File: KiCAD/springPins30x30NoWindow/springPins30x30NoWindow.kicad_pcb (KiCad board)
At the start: 2 copper layers, 30 x 30 mm, 22 parts, among them J1 CONN_02X06, J2 CONN_02X06

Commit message: wip commit
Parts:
- moved R1 22.7 mm to (5.08, -10.2), turned to 0 degrees
- moved J1 16.3 mm to (6.35, -3.81), turned to 90 degrees
- moved J2 2.54 mm to (6.35, 6.35), turned to 90 degrees
- moved JP1 0.65 mm to (4.45, 10.2), turned to 270 degrees
- turned L1 to 180 degrees
- turned L1 to 0 degrees
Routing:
- net /I2: track 6.99 -> 24.7 mm
- net /V5: track 6.99 -> 24.5 mm
- net /V2: track 6.99 -> 21.3 mm
- net /I5: track 6.99 -> 21.2 mm
- net /I4: track 6.99 -> 17.8 mm
- net /V3: track 6.99 -> 17.6 mm
- net /VT: track 17.5 -> 6.99 mm
- net /IB: track 17.5 -> 6.99 mm
- net /V4: track 6.99 -> 14.0 mm
- net /I3: track 6.99 -> 13.9 mm
- net /VB: track 13.8 -> 6.99 mm
- net /IT: track 13.1 -> 6.99 mm
- net /I6: track 6.99 -> 12.0 mm
- net /RL: track 8.61 -> 3.84 mm
- net /V1: track 6.99 -> 11.0 mm
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
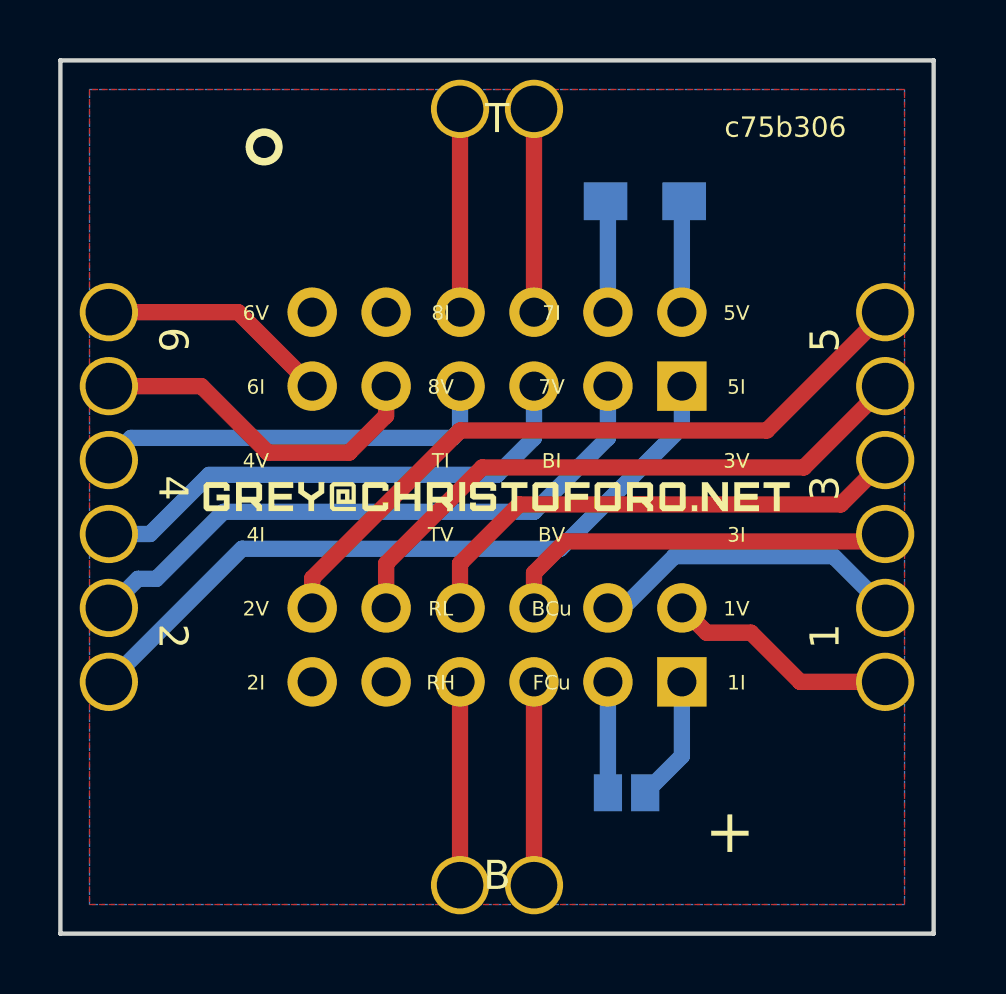
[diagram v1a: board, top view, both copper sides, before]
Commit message: rotate connectors on newMux
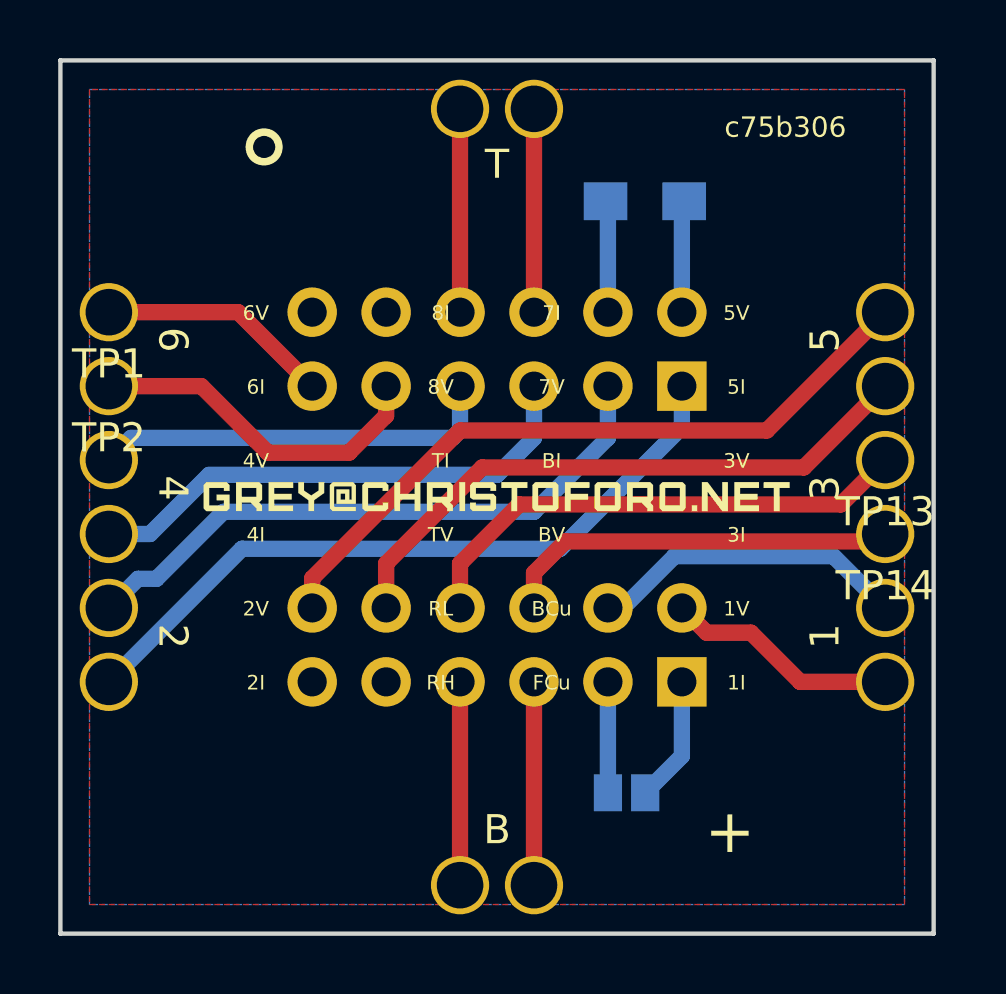
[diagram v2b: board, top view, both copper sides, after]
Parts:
- removed TP17, TP18, TP19, TP20: TEST, myParts:S25-022+P25-4023
- added TP1: TEST, myParts:S25-022+P25-4023, F.Cu at (-13.3, -6.35)
- added TP13: TEST, myParts:S25-022+P25-4023, F.Cu at (13.3, -1.27)
- added TP14: TEST, myParts:S25-022+P25-4023, F.Cu at (13.3, 1.27)
- added TP2: TEST, myParts:S25-022+P25-4023, F.Cu at (-13.3, -3.81)
- moved TP8 24.5 mm to (1.27, -13.3)
- moved TP12 21.0 mm to (13.3, -3.81)
- moved TP7 15.4 mm to (-1.27, 13.3)
- moved TP11 13.9 mm to (13.3, -6.35)
- moved TP15 10.2 mm to (13.3, 3.81)
- moved TP16 10.2 mm to (13.3, 6.35)
- moved TP3 5.08 mm to (-13.3, -1.27)
- moved TP4 5.08 mm to (-13.3, 1.27)
- moved TP5 5.08 mm to (-13.3, 3.81)
- moved TP6 5.08 mm to (-13.3, 6.35)
- moved TP10 2.54 mm to (1.27, 13.3)
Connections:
- TP10 pad 1: /IB -> /VB
- TP11 pad 1: /VT -> /V5
- TP12 pad 1: /VB -> /I5
- TP15 pad 1: /V5 -> /V1
- TP16 pad 1: /I5 -> /I1
- TP3 pad 1: /V6 -> /V4
- TP4 pad 1: /I6 -> /I4
- TP5 pad 1: /V4 -> /V2
- TP6 pad 1: /I4 -> /I2
- TP7 pad 1: /V2 -> /IB
- TP8 pad 1: /I2 -> /VT

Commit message: go back to old 30x30 springpins layout
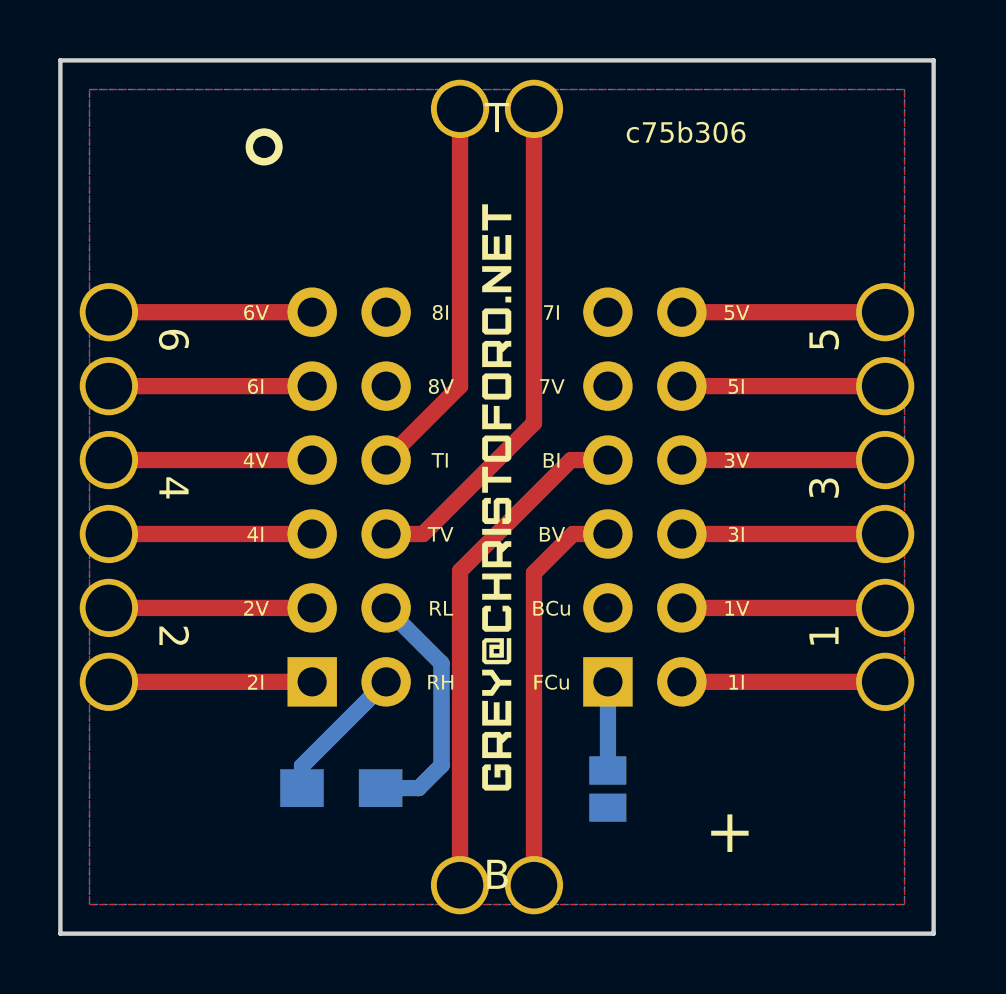
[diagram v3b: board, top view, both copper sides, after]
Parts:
- removed TP1, TP13, TP14, TP2: TEST, myParts:S25-022+P25-4023
- added TP17: TEST, myParts:S25-022+P25-4023, F.Cu at (13.3, -1.27)
- added TP18: TEST, myParts:S25-022+P25-4023, F.Cu at (13.3, 1.27)
- added TP19: TEST, myParts:S25-022+P25-4023, F.Cu at (13.3, 3.81)
- added TP20: TEST, myParts:S25-022+P25-4023, F.Cu at (13.3, 6.35)
- moved TP8 24.5 mm to (-13.3, 6.35)
- moved R1 22.7 mm to (-5.35, 10.0), turned to 180 degrees
- moved TP12 21.0 mm to (1.27, 13.3)
- moved J1 16.3 mm to (-6.35, 6.35), turned to 0 degrees
- moved TP7 15.4 mm to (-13.3, 3.81)
- moved TP11 13.9 mm to (1.27, -13.3)
- moved TP15 10.2 mm to (13.3, -6.35)
- moved TP16 10.2 mm to (13.3, -3.81)
- moved TP3 5.08 mm to (-13.3, -6.35)
- moved TP4 5.08 mm to (-13.3, -3.81)
- moved TP5 5.08 mm to (-13.3, -1.27)
- moved TP6 5.08 mm to (-13.3, 1.27)
- moved TP10 2.54 mm to (-1.27, 13.3)
- moved J2 2.54 mm to (3.81, 6.35), turned to 0 degrees
- moved JP1 0.65 mm to (3.81, 10.0), turned to 0 degrees
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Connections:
- TP10 pad 1: /VB -> /IB
- TP11 pad 1: /V5 -> /VT
- TP12 pad 1: /I5 -> /VB
- TP15 pad 1: /V1 -> /V5
- TP16 pad 1: /I1 -> /I5
- TP3 pad 1: /V4 -> /V6
- TP4 pad 1: /I4 -> /I6
- TP5 pad 1: /V2 -> /V4
- TP6 pad 1: /I2 -> /I4
- TP7 pad 1: /IB -> /V2
- TP8 pad 1: /VT -> /I2
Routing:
- net /I2: track 24.7 -> 6.99 mm
- net /V5: track 24.5 -> 6.99 mm
- net /V2: track 21.3 -> 6.99 mm
- net /I5: track 21.2 -> 6.99 mm
- net /I4: track 17.8 -> 6.99 mm
- net /V3: track 17.6 -> 6.99 mm
- net /VT: track 6.99 -> 17.5 mm
- net /IB: track 6.99 -> 17.5 mm
- net /V4: track 14.0 -> 6.99 mm
- net /I3: track 13.9 -> 6.99 mm
- net /VB: track 6.99 -> 13.8 mm
- net /IT: track 6.99 -> 13.1 mm
- net /I6: track 12.0 -> 6.99 mm
- net /RL: track 3.84 -> 8.61 mm
- net /V1: track 11.0 -> 6.99 mm
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
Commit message: spruce up spring pin boards
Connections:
- J1 pad 10: Net-(J1-Pad10) -> (no net)
- J1 pad 12: Net-(J1-Pad12) -> (no net)
- J2 pad 11: Net-(J2-Pad11) -> (no net)
- J2 pad 9: Net-(J2-Pad9) -> (no net)
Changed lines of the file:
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@@
-(kicad_pcb (version 20170123) (host pcbnew "(2017-09-19 revision 0083ce1bd)-master")
+(kicad_pcb (version 20171130) (host pcbnew "(5.0-dev-4060-g28f1209ce)")
   (general
     (thickness 1.6)
@@
     (zones 0)
     (modules 22)
-    (nets 25)
+    (nets 21)
   )
   (page A4)
@@
   (net 17 /VB)
   (net 18 /IB)
-  (net 19 "Net-(J1-Pad10)")
-  (net 20 "Net-(J1-Pad12)")
-  (net 21 /FCu)
-  (net 22 /BCu)
-  (net 23 "Net-(J2-Pad9)")
-  (net 24 "Net-(J2-Pad11)")
+  (net 19 /FCu)
+  (net 20 /BCu)
   (net_class Default "This is the default net class."
     (clearance 0.153)
@@
     (add_net /VB)
     (add_net /VT)
-    (add_net "Net-(J1-Pad10)")
-    (add_net "Net-(J1-Pad12)")
-    (add_net "Net-(J2-Pad11)")
-    (add_net "Net-(J2-Pad9)")
   )
   (module myParts:S25-022+P25-4023 (layer F.Cu)
@@
       (net 13 /I5))
     (model ${KIPRJMOD}/sharedLibs/myparts.3dshapes/S25-022+P25-4023.step
-      (at (xyz 0 0 0.2165354330708661))
+      (offset (xyz 0 0 5.499999917398286))
       (scale (xyz 1 1 1))
       (rotate (xyz -90 0 0))
@@
       (net 14 /V5))
     (model ${KIPRJMOD}/sharedLibs/myparts.3dshapes/S25-022+P25-4023.step
-      (at (xyz 0 0 0.2165354330708661))
+      (offset (xyz 0 0 5.499999917398286))
       (scale (xyz 1 1 1))
       (rotate (xyz -90 0 0))
@@
       (net 17 /VB))
     (model ${KIPRJMOD}/sharedLibs/myparts.3dshapes/S25-022+P25-4023.step
-      (at (xyz 0 0 0.2165354330708661))
+      (offset (xyz 0 0 5.499999917398286))
       (scale (xyz 1 1 1))
       (rotate (xyz -90 0 0))
@@
       (net 4 /VT))
     (model ${KIPRJMOD}/sharedLibs/myparts.3dshapes/S25-022+P25-4023.step
-      (at (xyz 0 0 0.2165354330708661))
+      (offset (xyz 0 0 5.499999917398286))
       (scale (xyz 1 1 1))
       (rotate (xyz -90 0 0))
@@
       (net 18 /IB))
     (model ${KIPRJMOD}/sharedLibs/myparts.3dshapes/S25-022+P25-4023.step
-      (at (xyz 0 0 0.2165354330708661))
+      (offset (xyz 0 0 5.499999917398286))
       (scale (xyz 1 1 1))
       (rotate (xyz -90 0 0))
@@
       (net 6 /IT))
     (model ${KIPRJMOD}/sharedLibs/myparts.3dshapes/S25-022+P25-4023.step
-      (at (xyz 0 0 0.2165354330708661))
+      (offset (xyz 0 0 5.499999917398286))
       (scale (xyz 1 1 1))
       (rotate (xyz -90 0 0))
@@
       (net 1 /I2))
     (model ${KIPRJMOD}/sharedLibs/myparts.3dshapes/S25-022+P25-4023.step
-      (at (xyz 0 0 0.2165354330708661))
+      (offset (xyz 0 0 5.499999917398286))
       (scale (xyz 1 1 1))
       (rotate (xyz -90 0 0))
@@
       (net 2 /V2))
     (model ${KIPRJMOD}/sharedLibs/myparts.3dshapes/S25-022+P25-4023.step
-      (at (xyz 0 0 0.2165354330708661))
+      (offset (xyz 0 0 5.499999917398286))
       (scale (xyz 1 1 1))
       (rotate (xyz -90 0 0))
@@
       (net 3 /I4))
     (model ${KIPRJMOD}/sharedLibs/myparts.3dshapes/S25-022+P25-4023.step
-      (at (xyz 0 0 0.2165354330708661))
+      (offset (xyz 0 0 5.499999917398286))
       (scale (xyz 1 1 1))
       (rotate (xyz -90 0 0))
@@
       (net 5 /V4))
     (model ${KIPRJMOD}/sharedLibs/myparts.3dshapes/S25-022+P25-4023.step
-      (at (xyz 0 0 0.2165354330708661))
+      (offset (xyz 0 0 5.499999917398286))
       (scale (xyz 1 1 1))
       (rotate (xyz -90 0 0))
@@
       (net 7 /I6))
     (model ${KIPRJMOD}/sharedLibs/myparts.3dshapes/S25-022+P25-4023.step
-      (at (xyz 0 0 0.2165354330708661))
+      (offset (xyz 0 0 5.499999917398286))
       (scale (xyz 1 1 1))
       (rotate (xyz -90 0 0))
@@
       (net 8 /V6))
     (model ${KIPRJMOD}/sharedLibs/myparts.3dshapes/S25-022+P25-4023.step
-      (at (xyz 0 0 0.2165354330708661))
+      (offset (xyz 0 0 5.499999917398286))
       (scale (xyz 1 1 1))
       (rotate (xyz -90 0 0))
@@
       (net 12 /V3))
     (model ${KIPRJMOD}/sharedLibs/myparts.3dshapes/S25-022+P25-4023.step
-      (at (xyz 0 0 0.2165354330708661))
+      (offset (xyz 0 0 5.499999917398286))
       (scale (xyz 1 1 1))
       (rotate (xyz -90 0 0))
@@
       (net 11 /I3))
     (model ${KIPRJMOD}/sharedLibs/myparts.3dshapes/S25-022+P25-4023.step
-      (at (xyz 0 0 0.2165354330708661))
+      (offset (xyz 0 0 5.499999917398286))
       (scale (xyz 1 1 1))
       (rotate (xyz -90 0 0))
@@
       (net 10 /V1))
     (model ${KIPRJMOD}/sharedLibs/myparts.3dshapes/S25-022+P25-4023.step
-      (at (xyz 0 0 0.2165354330708661))
+      (offset (xyz 0 0 5.499999917398286))
       (scale (xyz 1 1 1))
       (rotate (xyz -90 0 0))
@@
       (net 9 /I1))
     (model ${KIPRJMOD}/sharedLibs/myparts.3dshapes/S25-022+P25-4023.step
-      (at (xyz 0 0 0.2165354330708661))
+      (offset (xyz 0 0 5.499999917398286))
       (scale (xyz 1 1 1))
       (rotate (xyz -90 0 0))
@@
     (at 0 0 90)
     (fp_text reference L1 (at 0 4 90) (layer B.SilkS) hide
-      (effects (font (thickness 0.2)) (justify mirror))
+      (effects (font (size 1.524 1.524) (thickness 0.2)) (justify mirror))
     )
     (fp_text value GREY@CHRISTOFORO.NET (at 0 -4 90) (layer B.SilkS) hide
-      (effects (font (thickness 0.2)) (justify mirror))
+      (effects (font (size 1.524 1.524) (thickness 0.2)) (justify mirror))
     )
     (fp_poly (pts (xy -0.030446 0.410336) (xy -0.128951 0.511719) (xy -0.828528 0.511719) (xy -0.927058 0.410336)
@@
     )
     (pad 1 thru_hole rect (at 0 0) (size 1.7 1.7) (drill 1) (layers *.Cu *.Mask)
-      (net 21 /FCu))
+      (net 19 /FCu))
     (pad 2 thru_hole oval (at 2.54 0) (size 1.7 1.7) (drill 1) (layers *.Cu *.Mask)
       (net 9 /I1))
     (pad 3 thru_hole oval (at 0 -2.54) (size 1.7 1.7) (drill 1) (layers *.Cu *.Mask)
-      (net 22 /BCu))
+      (net 20 /BCu))
     (pad 4 thru_hole oval (at 2.54 -2.54) (size 1.7 1.7) (drill 1) (layers *.Cu *.Mask)
       (net 10 /V1))
@@
     (pad 8 thru_hole oval (at 2.54 -7.62) (size 1.7 1.7) (drill 1) (layers *.Cu *.Mask)
       (net 12 /V3))
-    (pad 9 thru_hole oval (at 0 -10.16) (size 1.7 1.7) (drill 1) (layers *.Cu *.Mask)
-      (net 23 "Net-(J2-Pad9)"))
+    (pad 9 thru_hole oval (at 0 -10.16) (size 1.7 1.7) (drill 1) (layers *.Cu *.Mask))
     (pad 10 thru_hole oval (at 2.54 -10.16) (size 1.7 1.7) (drill 1) (layers *.Cu *.Mask)
       (net 13 /I5))
-    (pad 11 thru_hole oval (at 0 -12.7) (size 1.7 1.7) (drill 1) (layers *.Cu *.Mask)
-      (net 24 "Net-(J2-Pad11)"))
+    (pad 11 thru_hole oval (at 0 -12.7) (size 1.7 1.7) (drill 1) (layers *.Cu *.Mask))
     (pad 12 thru_hole oval (at 2.54 -12.7) (size 1.7 1.7) (drill 1) (layers *.Cu *.Mask)
       (net 14 /V5))
@@
     (pad 9 thru_hole oval (at 0 -10.16) (size 1.7 1.7) (drill 1) (layers *.Cu *.Mask)
       (net 7 /I6))
-    (pad 10 thru_hole oval (at 2.54 -10.16) (size 1.7 1.7) (drill 1) (layers *.Cu *.Mask)
-      (net 19 "Net-(J1-Pad10)"))
+    (pad 10 thru_hole oval (at 2.54 -10.16) (size 1.7 1.7) (drill 1) (layers *.Cu *.Mask))
     (pad 11 thru_hole oval (at 0 -12.7) (size 1.7 1.7) (drill 1) (layers *.Cu *.Mask)
       (net 8 /V6))
-    (pad 12 thru_hole oval (at 2.54 -12.7) (size 1.7 1.7) (drill 1) (layers *.Cu *.Mask)
-      (net 20 "Net-(J1-Pad12)"))
+    (pad 12 thru_hole oval (at 2.54 -12.7) (size 1.7 1.7) (drill 1) (layers *.Cu *.Mask))
     (model ${KISYS3DMOD}/Pin_Headers.3dshapes/Pin_Header_Straight_2x06_Pitch2.54mm.wrl
       (at (xyz 0 0 0))
@@
     (at 0 0 90)
     (fp_text reference L1 (at 0 -4 90) (layer F.SilkS) hide
-      (effects (font (thickness 0.2)))
+      (effects (font (size 1.524 1.524) (thickness 0.2)))
     )
     (fp_text value GREY@CHRISTOFORO.NET (at 0 4 90) (layer F.SilkS) hide
-      (effects (font (thickness 0.2)))
+      (effects (font (size 1.524 1.524) (thickness 0.2)))
     )
     (fp_poly (pts (xy -0.030446 -0.410336) (xy -0.128951 -0.511719) (xy -0.828528 -0.511719) (xy -0.927058 -0.410336)
@@
     (fp_line (start -0.89 1.27) (end 0.89 1.27) (layer B.SilkS) (width 0.12))
     (pad 1 smd rect (at 0 0.64) (size 1.27 0.97) (layers B.Cu B.Paste B.Mask)
-      (net 22 /BCu))
+      (net 20 /BCu))
     (pad 2 smd rect (at 0 -0.64) (size 1.27 0.97) (layers B.Cu B.Paste B.Mask)
-      (net 21 /FCu))
+      (net 19 /FCu))
   )
   (gr_text 4I (at -8.285 1.3) (layer F.SilkS)
@@
   (segment (start -1.27 2.54) (end 2.54 -1.27) (width 0.56) (layer F.Cu) (net 18))
   (segment (start 2.54 -1.27) (end 3.81 -1.27) (width 0.56) (layer F.Cu) (net 18))
-  (segment (start 3.81 9.393) (end 3.81 6.35) (width 0.56) (layer B.Cu) (net 21))
-  (zone (net 22) (net_name /BCu) (layer B.Cu) (hatch edge 0.508)
+  (segment (start 3.81 9.393) (end 3.81 6.35) (width 0.56) (layer B.Cu) (net 19))
+  (zone (net 20) (net_name /BCu) (layer B.Cu) (hatch edge 0.508)
     (connect_pads (clearance 0.2))
     (min_thickness 0.254)
@@
     )
   )
-  (zone (net 21) (net_name /FCu) (layer F.Cu) (hatch edge 0.508)
+  (zone (net 19) (net_name /FCu) (layer F.Cu) (hatch edge 0.508)
     (connect_pads (clearance 0.2))
     (min_thickness 0.254)

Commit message: update silk
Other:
- board text added: "3ec2e93"
- board text removed: "c75b306"
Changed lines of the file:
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@@
     (effects (font (size 1 1) (thickness 0.25)))
   )
-  (gr_text c75b306 (at 6.5 -12.5) (layer F.SilkS)
-    (effects (font (size 0.7 0.7) (thickness 0.175)))
+  (gr_text 3ec2e93 (at 6.5 -12.5) (layer F.SilkS)
+    (effects (font (size 1 1) (thickness 0.175)))
   )
   (gr_text B (at 0 13) (layer F.SilkS)
